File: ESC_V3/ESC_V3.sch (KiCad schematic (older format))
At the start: 29 parts, among them J1 Conn_01x08_Male, J2 Conn_01x01_Male, J3 Conn_01x02_Male, J4 Conn_01x01_Male, J5 Conn_01x01_Male, Q1 MOSFET-NCH-2N7002PW, Q2 MOSFET-NCH-2N7002PW, Q3 MOSFET-NCH-2N7002PW, Q4 MOSFET-NCH-2N7002PW, Q5 MOSFET-NCH-2N7002PW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

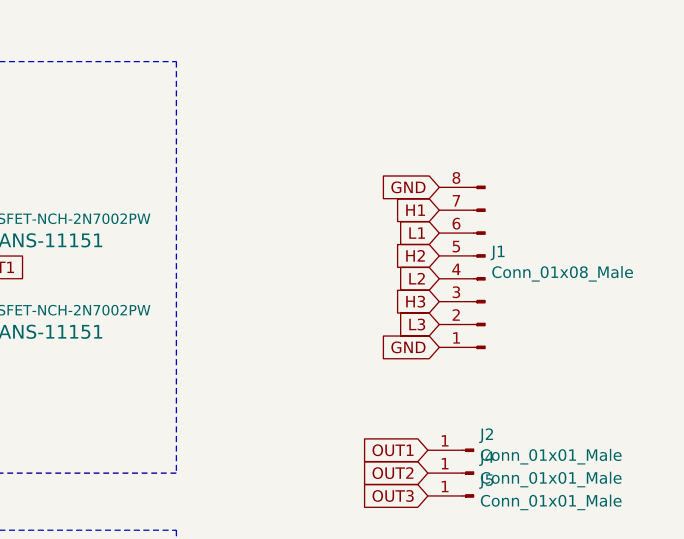
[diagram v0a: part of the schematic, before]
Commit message: Remap input pins to not be terrible
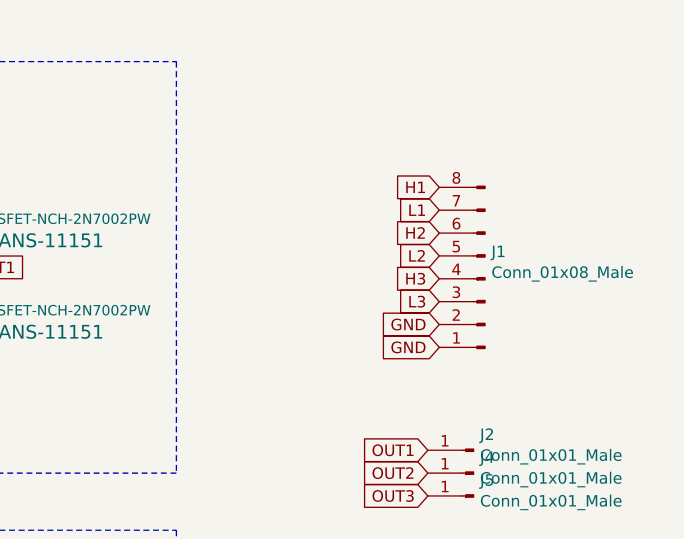
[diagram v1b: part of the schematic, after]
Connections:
- net GND: now also J1.2 (Pin_2); no longer J1.8 (Pin_8)
- net H1: now also J1.8 (Pin_8); no longer J1.7 (Pin_7)
- net H2: now also J1.6 (Pin_6); no longer J1.5 (Pin_5)
- net H3: now also J1.4 (Pin_4); no longer J1.3 (Pin_3)
- net L1: now also J1.7 (Pin_7); no longer J1.6 (Pin_6)
- net L2: now also J1.5 (Pin_5); no longer J1.4 (Pin_4)
- net L3: now also J1.3 (Pin_3); no longer J1.2 (Pin_2)
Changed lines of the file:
@@
 Text GLabel 5700 2150 0    50   Input ~ 0
 GND
+Text GLabel 5700 1950 0    50   Input ~ 0
+L3
+Text GLabel 5700 1850 0    50   Input ~ 0
+H3
+Text GLabel 5700 1750 0    50   Input ~ 0
+L2
+Text GLabel 5700 1650 0    50   Input ~ 0
+H2
+Text GLabel 5700 1550 0    50   Input ~ 0
+L1
+Text GLabel 5700 1450 0    50   Input ~ 0
+H1
 Text GLabel 5700 2050 0    50   Input ~ 0
-L3
-Text GLabel 5700 1950 0    50   Input ~ 0
-H3
-Text GLabel 5700 1850 0    50   Input ~ 0
-L2
-Text GLabel 5700 1750 0    50   Input ~ 0
-H2
-Text GLabel 5700 1650 0    50   Input ~ 0
-L1
-Text GLabel 5700 1550 0    50   Input ~ 0
-H1
-Text GLabel 5700 1450 0    50   Input ~ 0
 GND
 Text GLabel 5650 2600 0    50   Input ~ 0

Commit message: minor cleanup
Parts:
- Q1, Q2, Q3, Q4, Q5, Q6: symbol SparkFun-DiscreteSemi:MOSFET-NCH-2N7002PW -> ESC_V3-rescue:MOSFET-NCH-2N7002PW-SparkFun-DiscreteSemi
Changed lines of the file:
@@
 $EndComp
 $Comp
-L SparkFun-DiscreteSemi:MOSFET-NCH-2N7002PW Q1
+L ESC_V3-rescue:MOSFET-NCH-2N7002PW-SparkFun-DiscreteSemi Q1
 U 1 1 6114D7EA
 P 3500 1600
@@
 $EndComp
 $Comp
-L SparkFun-DiscreteSemi:MOSFET-NCH-2N7002PW Q2
+L ESC_V3-rescue:MOSFET-NCH-2N7002PW-SparkFun-DiscreteSemi Q2
 U 1 1 61150321
 P 3500 2000
@@
 $EndComp
 $Comp
-L SparkFun-DiscreteSemi:MOSFET-NCH-2N7002PW Q3
+L ESC_V3-rescue:MOSFET-NCH-2N7002PW-SparkFun-DiscreteSemi Q3
 U 1 1 6116C672
 P 3500 3650
@@
 $EndComp
 $Comp
-L SparkFun-DiscreteSemi:MOSFET-NCH-2N7002PW Q4
+L ESC_V3-rescue:MOSFET-NCH-2N7002PW-SparkFun-DiscreteSemi Q4
 U 1 1 6116C679
 P 3500 4050
@@
 $EndComp
 $Comp
-L SparkFun-DiscreteSemi:MOSFET-NCH-2N7002PW Q5
+L ESC_V3-rescue:MOSFET-NCH-2N7002PW-SparkFun-DiscreteSemi Q5
 U 1 1 61174DD5
 P 3500 5700
@@
 $EndComp
 $Comp
-L SparkFun-DiscreteSemi:MOSFET-NCH-2N7002PW Q6
+L ESC_V3-rescue:MOSFET-NCH-2N7002PW-SparkFun-DiscreteSemi Q6
 U 1 1 61174DDC
 P 3500 6100
